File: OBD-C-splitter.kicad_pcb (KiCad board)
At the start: 2 copper layers, 23 x 10.4 mm, 11 parts, among them J1 Type-C Plug, J2 Type-C Receptacle, J3 Type-C Receptacle

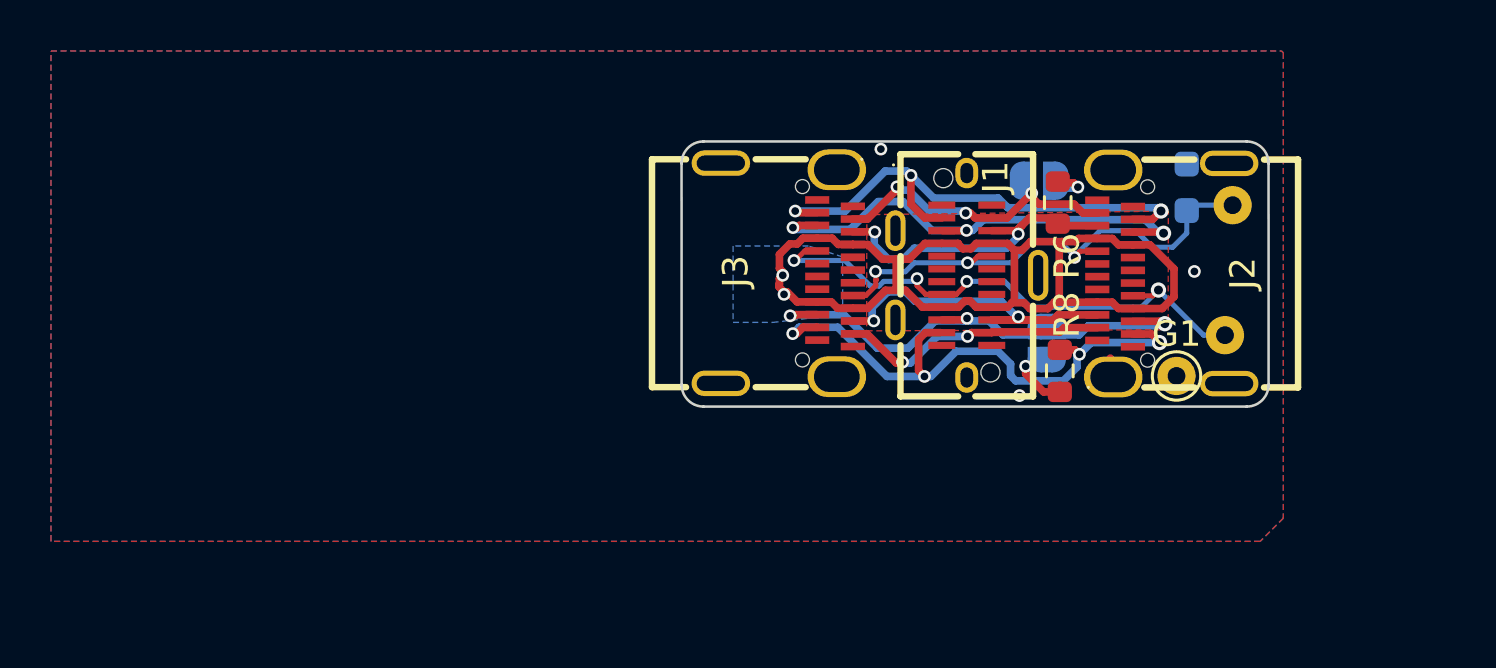
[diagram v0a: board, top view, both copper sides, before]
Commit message: Fixed CAN labels and termination resistors and sbu
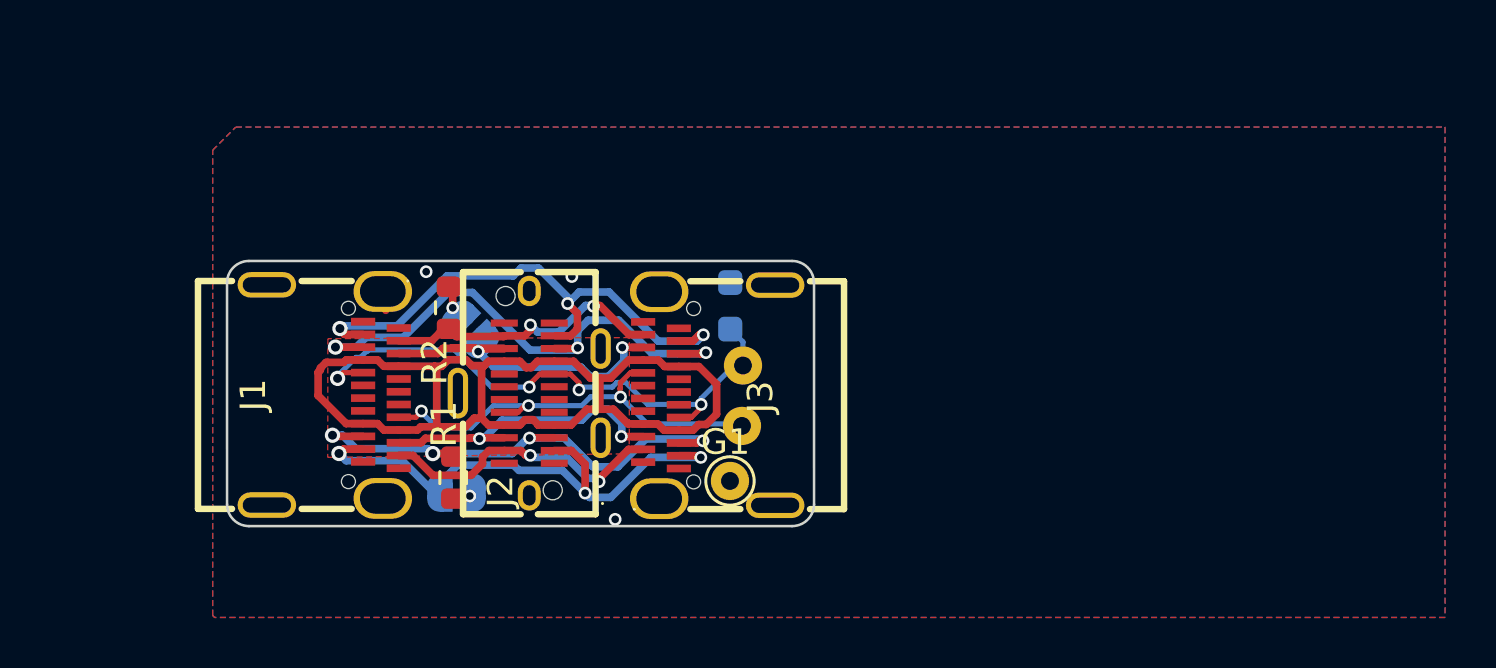
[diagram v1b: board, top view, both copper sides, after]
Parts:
- moved J1 32.9 mm to (101.4, 88.2), turned to -90 degrees
- moved R1 26.1 mm to (106.1, 91.5), turned to 90 degrees
- moved CAN1 25.9 mm to (106.2, 92.1)
- moved R2 24.1 mm to (106.0, 84.8), turned to 90 degrees
- moved CAN3 22.6 mm to (106.8, 85.7), turned to 135 degrees
- moved Ign1 21.1 mm to (117.5, 89.5), turned to 180 degrees
- moved Rly1 18.9 mm to (117.5, 87.1), turned to 180 degrees
- moved R3 18.5 mm to (117.0, 84.8)
- moved G1 18.0 mm to (117.0, 91.6), turned to 180 degrees
- moved J2 17.8 mm to (109.1, 88.2), turned to -90 degrees
- moved J3 5.67 mm to (116.2, 88.3), turned to 90 degrees
- renumbered SBU1 to Ign1, J2 to J1, J1 to J2, R6 to R1, R8 to R2, SBU3 to R3, SBU2 to Rly1
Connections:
- Ign1 pad 1: Net-(J1-SBU1) -> /Sbu2
- J1 pad A10: CAN1_L -> CAN2_L
- J1 pad A11: CAN1_H -> CAN2_H
- J1 pad A2: CAN0_H -> CAN3_H
- J1 pad A3: CAN0_L -> CAN3_L
- J1 pad A8: Net-(J1-SBU1) -> /Sbu2
- J1 pad B10: CAN3_L -> CAN0_L
- J1 pad B11: CAN3_H -> CAN0_H
- J1 pad B2: CAN2_H -> CAN1_H
- J1 pad B3: CAN2_L -> CAN1_L
- J1 pad B8: Net-(J1-SBU2) -> /Sbu1
- J2 pad A10: CAN1_L -> CAN2_L
- J2 pad A11: CAN1_H -> CAN2_H
- J2 pad A2: CAN0_H -> CAN3_H
- J2 pad A3: CAN0_L -> CAN3_L
- J2 pad A8: Net-(J1-SBU1) -> /Sbu2
- J2 pad B10: CAN3_L -> CAN0_L
- J2 pad B11: CAN3_H -> CAN0_H
- J2 pad B2: CAN2_H -> CAN1_H
- J2 pad B3: CAN2_L -> CAN1_L
- J2 pad B8: Net-(J1-SBU2) -> /Sbu1
- J3 pad A10: CAN2_L -> CAN1_L
- J3 pad A11: CAN2_H -> CAN1_H
- J3 pad A2: CAN3_H -> CAN0_H
- J3 pad A3: CAN3_L -> CAN0_L
- J3 pad A8: Net-(J1-SBU2) -> /Sbu1
- J3 pad B10: CAN0_L -> CAN3_L
- J3 pad B11: CAN0_H -> CAN3_H
- J3 pad B2: CAN1_H -> CAN2_H
- J3 pad B3: CAN1_L -> CAN2_L
- J3 pad B8: Net-(J1-SBU1) -> /Sbu2
- R3 pad 1: Net-(J1-SBU1) -> /Sbu1
- Rly1 pad 1: Net-(J1-SBU2) -> /Sbu1
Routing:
- net /Sbu1: track 0.00 -> 22.9 mm, vias 0 -> 4
- net Net-(J1-SBU2): track 21.6 -> 0.00 mm, vias 4 -> 0
- net Net-(J1-SBU1): track 20.4 -> 0.00 mm, vias 3 -> 0
- net /Sbu2: track 0.00 -> 17.6 mm, vias 0 -> 3
- net CAN3_H: track 23.0 -> 11.3 mm, vias 4 -> 2
- net CAN0_H: track 10.7 -> 21.3 mm, vias 2 -> 3
- net CAN1_H: track 12.1 -> 21.2 mm
- net CAN2_H: track 20.3 -> 11.5 mm, vias 3 -> 2
- net CAN1_L: track 12.6 -> 20.2 mm, vias 2 -> 4
- net CAN2_L: track 19.2 -> 12.0 mm, vias 3 -> 2
- net CAN0_L: track 14.3 -> 20.9 mm, vias 2 -> 3
- net CAN3_L: track 19.6 -> 14.3 mm, vias 3 -> 2
- net Net-(CAN3-B): track 2.20 -> 0.89 mm
- net Net-(CAN1-A): track 1.89 -> 0.69 mm
- net /VBUS: track 42.9 -> 42.8 mm, vias 2 -> 0
- removed copper zone on B.Cu, net /VBUS
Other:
- board text added: "Harness side"
- board text added: "rev.${REVISION}"
